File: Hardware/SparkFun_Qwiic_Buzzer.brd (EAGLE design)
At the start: 25.4 x 25.4 mm, 63 parts, among them J2 QWIIC_RA, J3 QWIIC_RA, Q3 200mA/40V, U4 ATTINY84-ARDUINO

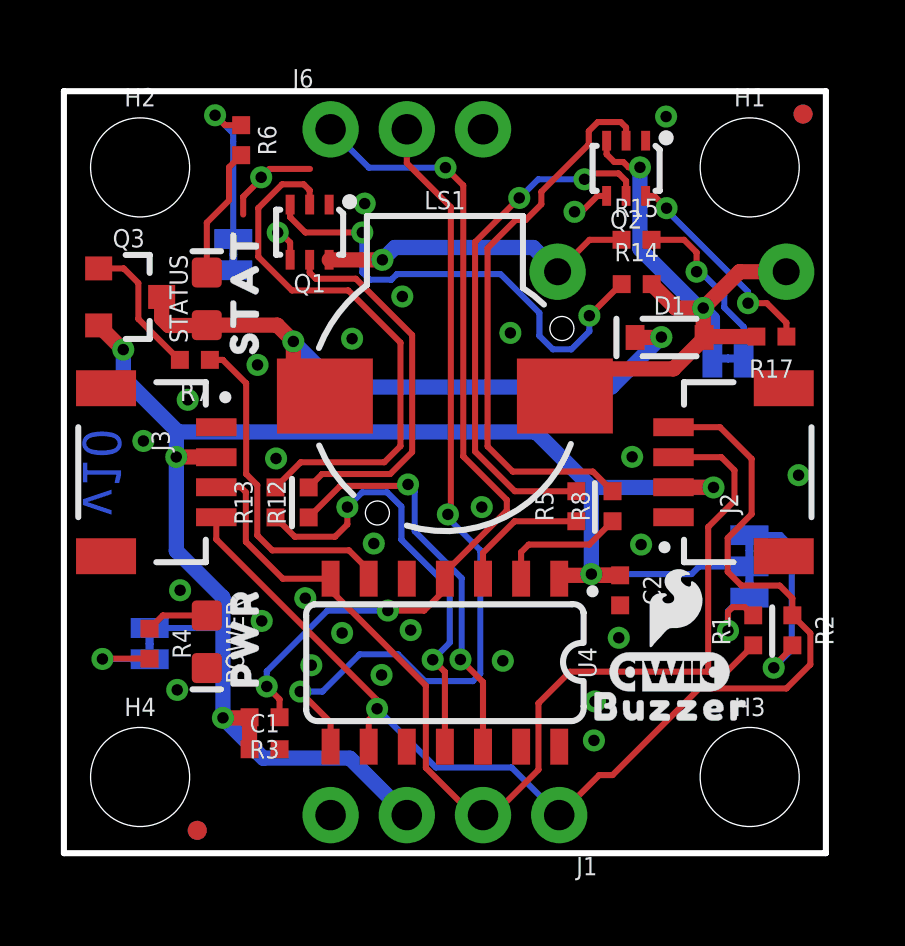
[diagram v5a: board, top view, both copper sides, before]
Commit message: STAT LED moved to GPIO
-This way it won't be dimmed by the buzzers frequency and can more precisely be controlled via firmware.
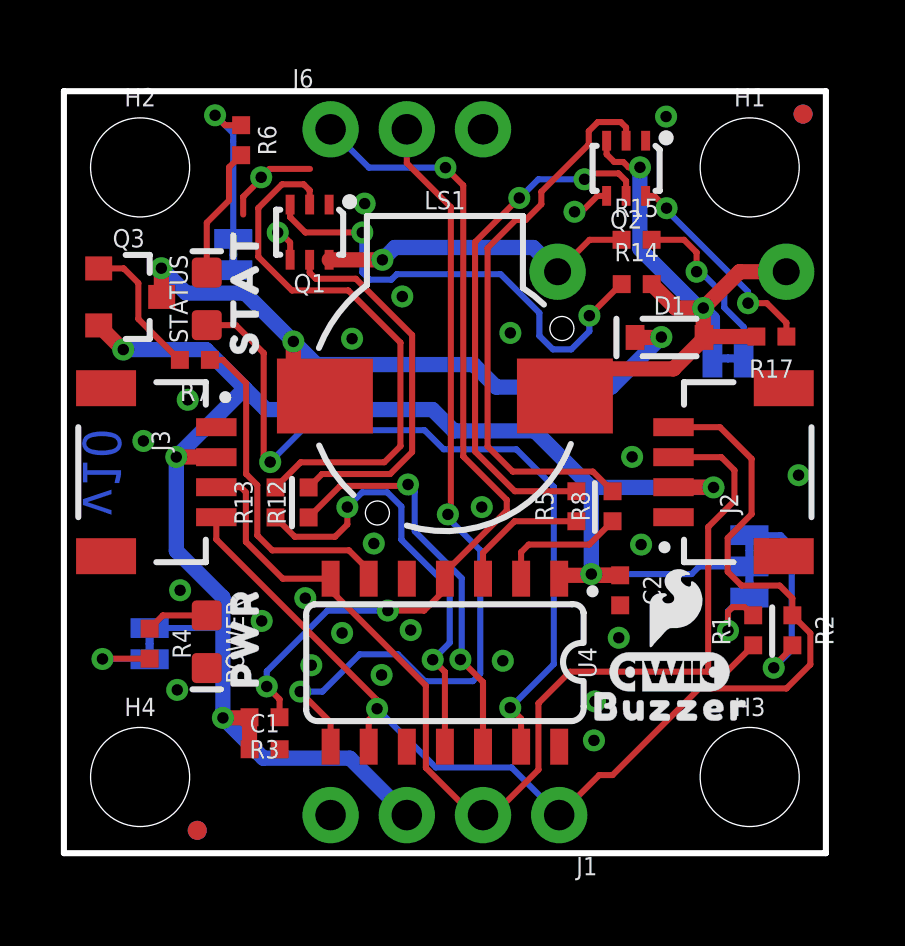
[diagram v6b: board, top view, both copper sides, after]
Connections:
- new net STAT: STATUS.A, U4.13
- net N$6: no longer STATUS.A
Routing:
- net STAT: track 0.00 -> 26.1 mm, vias 0 -> 2
- net 3.3V: track 59.3 -> 61.2 mm
- net N$6: track 22.2 -> 23.1 mm, vias 2 -> 3
- net GND: vias 29 -> 27
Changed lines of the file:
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@@
 <element name="J1" library="SparkFun-Connectors" package="1X04_NO_SILK" value="" x="16.51" y="1.27" smashed="yes" rot="R180">
 <attribute name="NAME" x="17.78" y="-0.127" size="0.6096" layer="25" font="vector" ratio="20" rot="R180"/>
-<attribute name="PROD_ID" value="CONN-09696" x="16.51" y="1.27" size="1.778" layer="27" font="vector" ratio="15" rot="R180" display="off"/>
+<attribute name="PROD_ID" value="" x="16.51" y="1.27" size="1.778" layer="27" font="vector" ratio="15" rot="R180" display="off"/>
 <attribute name="VALUE" x="17.78" y="3.302" size="0.6096" layer="27" font="vector" ratio="20" rot="R180"/>
 </element>
@@
 <via x="24.488140625" y="12.600940625" extent="1-16" drill="0.381"/>
 <via x="18.94078125" y="13.210540625" extent="1-16" drill="0.381"/>
-<via x="7.0713625" y="13.1572" extent="1-16" drill="0.381"/>
-<via x="6.45414375" y="16.27631875" extent="1-16" drill="0.381"/>
 <via x="2.649225" y="13.7414" extent="1-16" drill="0.381"/>
 <via x="6.59384375" y="7.741921875" extent="1-16" drill="0.381"/>
@@
 <via x="17.58188125" y="9.304021875" extent="1-16" drill="0.381"/>
 <wire x1="17.58188125" y1="9.304021875" x2="17.58188125" y2="12.192" width="0.508" layer="16"/>
-<wire x1="3.7465" y1="13.208" x2="3.7465" y2="14.041121875" width="0.508" layer="16"/>
-<wire x1="3.7465" y1="14.041121875" x2="3.7465" y2="14.097" width="0.508" layer="16"/>
 <via x="1.978659375" y="16.786859375" extent="1-16" drill="0.381"/>
 <wire x1="1.159" y1="17.592" x2="1.964140625" y2="16.786859375" width="0.508" layer="1"/>
@@
 <wire x1="5.30098125" y1="8.5242375" x2="5.30098125" y2="7.508240625" width="0.508" layer="16"/>
 <wire x1="3.7465" y1="10.07871875" x2="5.30098125" y2="8.5242375" width="0.508" layer="16"/>
-<wire x1="1.978659375" y1="16.786859375" x2="1.978659375" y2="15.864840625" width="0.508" layer="16"/>
-<wire x1="1.978659375" y1="15.864840625" x2="3.7465" y2="14.097" width="0.508" layer="16"/>
 <wire x1="22.849840625" y1="9.5605625" x2="21.178521875" y2="9.5605625" width="0.2032" layer="16"/>
-<wire x1="20.92198125" y1="9.304021875" x2="19.79168125" y2="9.304021875" width="0.2032" layer="16"/>
-<wire x1="19.79168125" y1="9.304021875" x2="17.58188125" y2="9.304021875" width="0.2032" layer="16"/>
+<wire x1="20.92198125" y1="9.304021875" x2="17.58188125" y2="9.304021875" width="0.2032" layer="16"/>
 <wire x1="21.178521875" y1="9.5605625" x2="20.92198125" y2="9.304021875" width="0.2032" layer="16"/>
 <contactref element="C1" pad="1"/>
 <wire x1="6.18781875" y1="4.531359375" x2="6.18781875" y2="3.467103125" width="0.508" layer="1"/>
 <wire x1="6.18781875" y1="3.467103125" x2="6.190359375" y2="3.4645625" width="0.508" layer="1"/>
-<wire x1="15.732759375" y1="14.041121875" x2="17.58188125" y2="12.192" width="0.508" layer="16"/>
-<wire x1="3.7465" y1="14.041121875" x2="15.732759375" y2="14.041121875" width="0.508" layer="16"/>
 <wire x1="11.43" y1="1.27" x2="9.53261875" y2="3.16738125" width="0.508" layer="16"/>
 <wire x1="6.644640625" y1="3.16738125" x2="5.30098125" y2="4.511040625" width="0.508" layer="16"/>
 <wire x1="9.53261875" y1="3.16738125" x2="6.644640625" y2="3.16738125" width="0.508" layer="16"/>
+<wire x1="4.737103125" y1="16.786859375" x2="1.978659375" y2="16.786859375" width="0.508" layer="16"/>
+<wire x1="6.03123125" y1="15.49273125" x2="4.737103125" y2="16.786859375" width="0.508" layer="16"/>
+<wire x1="3.7465" y1="13.208" x2="6.03123125" y2="15.49273125" width="0.508" layer="16"/>
+<wire x1="12.99971875" y1="14.07668125" x2="12.28851875" y2="14.78788125" width="0.508" layer="16"/>
+<wire x1="17.58188125" y1="12.192" x2="15.6972" y2="14.07668125" width="0.508" layer="16"/>
+<wire x1="15.6972" y1="14.07668125" x2="12.99971875" y2="14.07668125" width="0.508" layer="16"/>
+<wire x1="12.28851875" y1="14.78788125" x2="6.73608125" y2="14.78788125" width="0.508" layer="16"/>
+<wire x1="6.73608125" y1="14.78788125" x2="6.03123125" y2="15.49273125" width="0.508" layer="16"/>
 </signal>
 <signal name="3.3V1">
@@
 <contactref element="LS1" pad="+"/>
 <contactref element="Q3" pad="3"/>
-<contactref element="STATUS" pad="A"/>
-<wire x1="3.259" y1="18.542" x2="3.259" y2="17.823" width="0.508" layer="1"/>
-<wire x1="3.259" y1="17.823" x2="3.4925" y2="17.5895" width="0.508" layer="1"/>
-<wire x1="3.4925" y1="17.5895" x2="4.7505" y2="17.5895" width="0.508" layer="1"/>
-<wire x1="4.7505" y1="17.5895" x2="4.7625" y2="17.6015" width="0.508" layer="1"/>
 <contactref element="D1" pad="C"/>
 <wire x1="19.9161375" y1="17.203415625" x2="19.9034375" y2="17.190715625" width="0.508" layer="1"/>
@@
 <via x="19.9161375" y="17.203415625" extent="1-16" drill="0.381"/>
 <wire x1="19.9161375" y1="17.203415625" x2="18.249903125" y2="15.53718125" width="0.508" layer="16"/>
-<wire x1="7.6479375" y1="17.040859375" x2="7.6479375" y2="17.058640625" width="0.508" layer="16"/>
 <via x="7.6479375" y="17.058640625" extent="1-16" drill="0.381"/>
 <wire x1="7.6479375" y1="17.058640625" x2="7.648440625" y2="17.058640625" width="0.508" layer="1"/>
 <wire x1="7.648440625" y1="17.058640625" x2="7.648440625" y2="16.291559375" width="0.508" layer="1"/>
 <wire x1="7.648440625" y1="16.291559375" x2="8.7" y2="15.24" width="0.508" layer="1"/>
-<wire x1="18.249903125" y1="15.53718125" x2="9.151615625" y2="15.53718125" width="0.508" layer="16"/>
-<wire x1="9.151615625" y1="15.53718125" x2="7.6479375" y2="17.040859375" width="0.508" layer="16"/>
-<wire x1="7.6479375" y1="17.058640625" x2="7.6479375" y2="17.066259375" width="0.508" layer="1"/>
-<wire x1="7.6479375" y1="17.066259375" x2="7.112696875" y2="17.6015" width="0.508" layer="1"/>
-<wire x1="4.7625" y1="17.6015" x2="7.112696875" y2="17.6015" width="0.508" layer="1"/>
+<via x="3.248659375" y="19.49958125" extent="1-16" drill="0.381"/>
+<wire x1="7.6479375" y1="17.058640625" x2="6.035040625" y2="18.6715375" width="0.508" layer="16"/>
+<wire x1="6.035040625" y1="18.6715375" x2="4.07310625" y2="18.6715375" width="0.508" layer="16"/>
+<wire x1="4.07310625" y1="18.6715375" x2="3.248659375" y2="19.495984375" width="0.508" layer="16"/>
+<wire x1="3.248659375" y1="19.49958125" x2="3.248659375" y2="19.495984375" width="0.508" layer="16"/>
+<wire x1="3.248659375" y1="19.49958125" x2="3.248659375" y2="18.552340625" width="0.508" layer="1"/>
+<wire x1="3.248659375" y1="18.552340625" x2="3.259" y2="18.542" width="0.508" layer="1"/>
+<wire x1="18.249903125" y1="15.53718125" x2="14.40941875" y2="15.53718125" width="0.508" layer="16"/>
+<wire x1="13.658853125" y1="16.287746875" x2="10.16" y2="16.287746875" width="0.508" layer="16"/>
+<wire x1="10.16" y1="16.287746875" x2="9.67105" y2="16.287746875" width="0.508" layer="16"/>
+<wire x1="14.40941875" y1="15.53718125" x2="13.658853125" y2="16.287746875" width="0.508" layer="16"/>
+<wire x1="9.67105" y1="16.287746875" x2="8.41883125" y2="16.287746875" width="0.508" layer="16"/>
+<wire x1="8.41883125" y1="16.287746875" x2="7.6479375" y2="17.058640625" width="0.508" layer="16"/>
 </signal>
 <signal name="VOL_0">
@@
 <wire x1="20.670521875" y1="20.447" x2="21.08961875" y2="20.027903125" width="0.2032" layer="1"/>
 </signal>
+<signal name="STAT">
+<contactref element="STATUS" pad="A"/>
+<wire x1="4.7625" y1="17.6015" x2="5.730940625" y2="17.6015" width="0.2032" layer="1"/>
+<wire x1="6.65988125" y1="13.253996875" x2="6.87578125" y2="13.038096875" width="0.2032" layer="1"/>
+<via x="6.87578125" y="13.038096875" extent="1-16" drill="0.381"/>
+<wire x1="15.08224375" y1="13.462275" x2="16.329659375" y2="12.214859375" width="0.2032" layer="16"/>
+<wire x1="16.329659375" y1="12.214859375" x2="16.329659375" y2="6.3017375" width="0.2032" layer="16"/>
+<wire x1="5.730940625" y1="17.6015" x2="6.65988125" y2="16.672559375" width="0.2032" layer="1"/>
+<wire x1="6.65988125" y1="16.672559375" x2="6.65988125" y2="13.253996875" width="0.2032" layer="1"/>
+<contactref element="U4" pad="13"/>
+<wire x1="15.24" y1="3.55" x2="15.24" y2="4.485640625" width="0.2032" layer="1"/>
+<wire x1="15.24" y1="4.485640625" x2="14.87678125" y2="4.848859375" width="0.2032" layer="1"/>
+<via x="14.87678125" y="4.848859375" extent="1-16" drill="0.381"/>
+<wire x1="14.87678125" y1="4.848859375" x2="16.329659375" y2="6.3017375" width="0.2032" layer="16"/>
+<wire x1="12.6590875" y1="13.462275" x2="15.08224375" y2="13.462275" width="0.2032" layer="16"/>
+<wire x1="6.87578125" y1="13.038096875" x2="7.939765625" y2="14.10208125" width="0.2032" layer="16"/>
+<wire x1="7.939765625" y1="14.10208125" x2="12.01928125" y2="14.10208125" width="0.2032" layer="16"/>
+<wire x1="12.01928125" y1="14.10208125" x2="12.6590875" y2="13.462275" width="0.2032" layer="16"/>
+</signal>
 </signals>

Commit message: routing nudges
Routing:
- net N$10: track 18.3 -> 17.4 mm
- net N$11: track 12.5 -> 11.7 mm
- net STAT: track 26.1 -> 25.5 mm
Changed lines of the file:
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@@
 <contactref element="Q1" pad="2"/>
 <contactref element="R13" pad="2"/>
-<wire x1="7.053578125" y1="12.192" x2="7.89178125" y2="13.030203125" width="0.2032" layer="1"/>
-<wire x1="10.680703125" y1="13.030203125" x2="11.21918125" y2="13.56868125" width="0.2032" layer="1"/>
-<wire x1="11.21918125" y1="13.56868125" x2="11.21918125" y2="17.018" width="0.2032" layer="1"/>
+<wire x1="7.053578125" y1="12.192" x2="8.48868125" y2="13.627103125" width="0.2032" layer="1"/>
+<wire x1="10.416546875" y1="13.627103125" x2="10.7315" y2="13.94205625" width="0.2032" layer="1"/>
+<wire x1="10.7315" y1="13.94205625" x2="10.7315" y2="17.50568125" width="0.2032" layer="1"/>
 <wire x1="7.272021875" y1="22.296121875" x2="7.993378125" y2="22.296121875" width="0.2032" layer="1"/>
 <wire x1="7.993378125" y1="22.296121875" x2="8.1915" y2="22.098" width="0.2032" layer="1"/>
 <wire x1="8.1915" y1="22.098" x2="8.1915" y2="21.621" width="0.2032" layer="1"/>
-<wire x1="7.89178125" y1="13.030203125" x2="10.680703125" y2="13.030203125" width="0.2032" layer="1"/>
+<wire x1="8.48868125" y1="13.627103125" x2="10.416546875" y2="13.627103125" width="0.2032" layer="1"/>
 <wire x1="6.47954375" y1="19.880571875" x2="6.47954375" y2="21.50364375" width="0.2032" layer="1"/>
 <wire x1="6.47954375" y1="21.50364375" x2="7.272021875" y2="22.296121875" width="0.2032" layer="1"/>
-<wire x1="11.21918125" y1="17.018" x2="9.47928125" y2="18.7579" width="0.2032" layer="1"/>
+<wire x1="10.7315" y1="17.50568125" x2="9.47928125" y2="18.7579" width="0.2032" layer="1"/>
 <wire x1="9.47928125" y1="18.7579" x2="7.602215625" y2="18.7579" width="0.2032" layer="1"/>
 <wire x1="7.602215625" y1="18.7579" x2="6.47954375" y2="19.880571875" width="0.2032" layer="1"/>
@@
 <contactref element="Q1" pad="5"/>
 <contactref element="R12" pad="2"/>
-<wire x1="10.876278125" y1="12.639040625" x2="8.60551875" y2="12.639040625" width="0.2032" layer="1"/>
-<wire x1="8.158478125" y1="12.192" x2="8.60551875" y2="12.639040625" width="0.2032" layer="1"/>
-<wire x1="10.876278125" y1="12.639040625" x2="11.6078" y2="13.3705625" width="0.2032" layer="1"/>
-<wire x1="11.6078" y1="13.3705625" x2="11.6078" y2="17.272" width="0.2032" layer="1"/>
+<wire x1="10.612121875" y1="13.16481875" x2="9.131296875" y2="13.16481875" width="0.2032" layer="1"/>
+<wire x1="8.158478125" y1="12.192" x2="9.131296875" y2="13.16481875" width="0.2032" layer="1"/>
+<wire x1="10.612121875" y1="13.16481875" x2="11.183621875" y2="13.73631875" width="0.2032" layer="1"/>
+<wire x1="11.183621875" y1="13.73631875" x2="11.183621875" y2="17.696178125" width="0.2032" layer="1"/>
 <wire x1="9.730740625" y1="19.149059375" x2="8.397240625" y2="19.149059375" width="0.2032" layer="1"/>
 <wire x1="8.397240625" y1="19.149059375" x2="8.1915" y2="19.3548" width="0.2032" layer="1"/>
 <wire x1="8.1915" y1="19.3548" x2="8.1915" y2="19.781" width="0.2032" layer="1"/>
-<wire x1="11.6078" y1="17.272" x2="9.730740625" y2="19.149059375" width="0.2032" layer="1"/>
+<wire x1="11.183621875" y1="17.696178125" x2="9.730740625" y2="19.149059375" width="0.2032" layer="1"/>
 </signal>
 <signal name="N$12">
@@
 <contactref element="R12" pad="1"/>
 <contactref element="U4" pad="12"/>
-<wire x1="8.158478125" y1="11.192" x2="9.210040625" y2="12.2435625" width="0.2032" layer="1"/>
-<wire x1="11.4706375" y1="12.29105625" x2="11.42314375" y2="12.2435625" width="0.2032" layer="1"/>
-<wire x1="11.42314375" y1="12.2435625" x2="9.210040625" y2="12.2435625" width="0.2032" layer="1"/>
-<via x="11.4706375" y="12.29105625" extent="1-16" drill="0.381"/>
-<wire x1="13.261340625" y1="9.166865625" x2="11.69415625" y2="10.73405" width="0.2032" layer="16"/>
-<wire x1="11.4706375" y1="12.29105625" x2="11.69415625" y2="12.0675375" width="0.2032" layer="16"/>
-<wire x1="11.69415625" y1="12.0675375" x2="11.69415625" y2="10.73405" width="0.2032" layer="16"/>
+<wire x1="8.158478125" y1="11.192" x2="9.2557625" y2="12.289284375" width="0.2032" layer="1"/>
+<wire x1="11.427459375" y1="12.2961375" x2="11.42060625" y2="12.289284375" width="0.2032" layer="1"/>
+<wire x1="11.42060625" y1="12.289284375" x2="9.2557625" y2="12.289284375" width="0.2032" layer="1"/>
+<via x="11.427459375" y="12.2961375" extent="1-16" drill="0.381"/>
+<wire x1="13.261340625" y1="9.166865625" x2="11.574775" y2="10.85343125" width="0.2032" layer="16"/>
+<wire x1="11.427459375" y1="12.2961375" x2="11.574775" y2="12.148821875" width="0.2032" layer="16"/>
+<wire x1="11.574775" y1="12.148821875" x2="11.574775" y2="10.85343125" width="0.2032" layer="16"/>
 <wire x1="13.261340625" y1="9.166865625" x2="13.261340625" y2="6.499859375" width="0.2032" layer="16"/>
 <wire x1="13.261340625" y1="6.499859375" x2="13.2181625" y2="6.45668125" width="0.2032" layer="16"/>
@@
 <contactref element="R13" pad="1"/>
 <contactref element="U4" pad="11"/>
-<wire x1="9.037321875" y1="10.548621875" x2="7.69695625" y2="10.548621875" width="0.2032" layer="1"/>
+<wire x1="8.986521875" y1="10.548621875" x2="7.69695625" y2="10.548621875" width="0.2032" layer="1"/>
 <wire x1="7.053578125" y1="11.192" x2="7.69695625" y2="10.548621875" width="0.2032" layer="1"/>
-<wire x1="9.4488" y1="11.53668125" x2="9.4488" y2="10.9601" width="0.2032" layer="1"/>
-<wire x1="9.4488" y1="10.9601" x2="9.037321875" y2="10.548621875" width="0.2032" layer="1"/>
+<wire x1="9.4488" y1="11.53668125" x2="9.4488" y2="11.0109" width="0.2032" layer="1"/>
+<wire x1="9.4488" y1="11.0109" x2="8.986521875" y2="10.548621875" width="0.2032" layer="1"/>
 <via x="9.4488" y="11.53668125" extent="1-16" drill="0.381"/>
 <wire x1="12.293596875" y1="6.449059375" x2="12.862559375" y2="7.018021875" width="0.2032" layer="16"/>
@@
 <wire x1="12.7" y1="6.04265625" x2="12.7" y2="3.55" width="0.2032" layer="1"/>
 <wire x1="12.862559375" y1="8.836659375" x2="12.862559375" y2="7.018021875" width="0.2032" layer="16"/>
-<wire x1="9.4488" y1="11.53668125" x2="9.94155625" y2="12.0294375" width="0.2032" layer="16"/>
-<wire x1="10.77468125" y1="12.0294375" x2="11.249659375" y2="11.554459375" width="0.2032" layer="16"/>
-<wire x1="11.249659375" y1="11.554459375" x2="11.249659375" y2="10.449559375" width="0.2032" layer="16"/>
-<wire x1="11.249659375" y1="10.449559375" x2="12.862559375" y2="8.836659375" width="0.2032" layer="16"/>
-<wire x1="9.94155625" y1="12.0294375" x2="10.77468125" y2="12.0294375" width="0.2032" layer="16"/>
+<wire x1="9.4488" y1="11.53668125" x2="9.949178125" y2="12.037059375" width="0.2032" layer="16"/>
+<wire x1="10.716259375" y1="12.037059375" x2="11.1633" y2="11.59001875" width="0.2032" layer="16"/>
+<wire x1="11.1633" y1="11.59001875" x2="11.1633" y2="10.53591875" width="0.2032" layer="16"/>
+<wire x1="11.1633" y1="10.53591875" x2="12.862559375" y2="8.836659375" width="0.2032" layer="16"/>
+<wire x1="9.949178125" y1="12.037059375" x2="10.716259375" y2="12.037059375" width="0.2032" layer="16"/>
 </signal>
 <signal name="N$13">
@@
 <signal name="STAT">
 <contactref element="STATUS" pad="A"/>
-<wire x1="4.7625" y1="17.6015" x2="5.730940625" y2="17.6015" width="0.2032" layer="1"/>
-<wire x1="6.65988125" y1="13.253996875" x2="6.87578125" y2="13.038096875" width="0.2032" layer="1"/>
-<via x="6.87578125" y="13.038096875" extent="1-16" drill="0.381"/>
+<wire x1="6.8173625" y1="13.055878125" x2="6.814821875" y2="13.0533375" width="0.2032" layer="1"/>
+<via x="6.814821875" y="13.0533375" extent="1-16" drill="0.381"/>
 <wire x1="15.08224375" y1="13.462275" x2="16.329659375" y2="12.214859375" width="0.2032" layer="16"/>
 <wire x1="16.329659375" y1="12.214859375" x2="16.329659375" y2="6.3017375" width="0.2032" layer="16"/>
-<wire x1="5.730940625" y1="17.6015" x2="6.65988125" y2="16.672559375" width="0.2032" layer="1"/>
-<wire x1="6.65988125" y1="16.672559375" x2="6.65988125" y2="13.253996875" width="0.2032" layer="1"/>
+<wire x1="6.8173625" y1="15.5448" x2="4.7625" y2="17.5996625" width="0.2032" layer="1"/>
+<wire x1="4.7625" y1="17.6015" x2="4.7625" y2="17.5996625" width="0.2032" layer="1"/>
+<wire x1="6.8173625" y1="15.5448" x2="6.8173625" y2="13.055878125" width="0.2032" layer="1"/>
 <contactref element="U4" pad="13"/>
 <wire x1="15.24" y1="3.55" x2="15.24" y2="4.485640625" width="0.2032" layer="1"/>
@@
 <wire x1="14.87678125" y1="4.848859375" x2="16.329659375" y2="6.3017375" width="0.2032" layer="16"/>
 <wire x1="12.6590875" y1="13.462275" x2="15.08224375" y2="13.462275" width="0.2032" layer="16"/>
-<wire x1="6.87578125" y1="13.038096875" x2="7.939765625" y2="14.10208125" width="0.2032" layer="16"/>
-<wire x1="7.939765625" y1="14.10208125" x2="12.01928125" y2="14.10208125" width="0.2032" layer="16"/>
+<wire x1="6.814821875" y1="13.0533375" x2="7.863565625" y2="14.10208125" width="0.2032" layer="16"/>
+<wire x1="7.863565625" y1="14.10208125" x2="12.01928125" y2="14.10208125" width="0.2032" layer="16"/>
 <wire x1="12.01928125" y1="14.10208125" x2="12.6590875" y2="13.462275" width="0.2032" layer="16"/>
 </signal>

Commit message: final review tweaks - no copper changes
-re-order position of 0.1uF and 10uF Caps
-re-order vol resistors
-redo measures so they are better
-added QWIIC logo to sch
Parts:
- LOGO5: value (none) -> QWIIC_LOGO_4MM
- R15: value 100 -> 2.2k
- R17: value 2.2k -> 100
- moved FRAME1 93.8 mm to (74.9, -8.89)
- moved LOGO3 1.27 mm to (57.1, 52.1)
- renumbered U$3 to LOGO5
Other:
- board text added: "Thickness: 1.6mm Layers: 2 Solder Mask Color: Red Silkscreen: White Finish: Lead-Free HASL Material: TG135-140 Copper Plating: 1oz"
- board text removed: "Thickness: 1.6mm Layers: 2 Solder Mask Color: Red Silkscreen: White Finish: Lead-Free HASL Material: TG135-140 Copper Plating: 1OZ"
